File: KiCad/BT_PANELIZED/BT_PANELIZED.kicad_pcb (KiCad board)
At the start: 4 copper layers, 82 x 63.6 mm, 482 parts, among them J1 UJC-HP-3-SMT-TR, J2 2328702-8, J3 Conn_01x05, SW1 Val**, U1 QFN40P120X130X45-6N, U2 SON95P300X300X100-7N-D, U3 STM6601CQ2BDM6F, U4 BMD-350-A-R, U5 UDFN6, U6 UDFN6, U7 UDFN6, Y1 ECS-.327-7-34R-TR

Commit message: updated
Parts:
- removed the C10 at (113.7, 57.4)
- removed the C10 at (148.2, 57.4)
- removed the C10 at (113.7, 74.2)
- removed the C10 at (148.2, 40.6)
- removed the C10 at (113.7, 40.6)
- removed the C10 at (148.2, 74.2)
- removed the C12 at (113.7, 39.6)
- removed the C12 at (148.2, 39.6)
- removed the C12 at (113.7, 73.1)
- removed the C12 at (148.2, 73.1)
- removed the C12 at (148.2, 56.3)
- removed the C12 at (113.7, 56.3)
- removed the C13 at (113.7, 72.0)
- removed the C13 at (148.2, 38.5)
- removed the C13 at (113.7, 38.5)
- removed the C13 at (148.2, 72.0)
- removed the C13 at (113.7, 55.2)
- removed the C13 at (148.2, 55.2)
- removed the C2 at (120.7, 55.7)
- removed the C2 at (155.2, 38.9)
- removed the C2 at (155.2, 72.4)
- removed the C2 at (120.7, 72.4)
- removed the C2 at (120.7, 38.9)
- removed the C2 at (155.2, 55.7)
- removed the C8 at (146.2, 57.5)
- removed the C8 at (111.7, 57.5)
- removed the C8 at (111.7, 74.2)
- removed the C8 at (146.2, 40.7)
- removed the C8 at (146.2, 74.2)
- removed the C8 at (111.7, 40.7)
- removed the C9 at (109.7, 40.7)
- removed the C9 at (144.2, 57.5)
- removed the C9 at (144.2, 74.2)
- removed the C9 at (109.7, 74.2)
- removed the C9 at (109.7, 57.5)
- removed the C9 at (144.2, 40.7)
- removed the D3 at (126.9, 50.6)
- removed the D3 at (126.9, 84.2)
- removed the D3 at (161.4, 84.2)
- removed the D3 at (161.4, 67.4)
- removed the D3 at (126.9, 67.4)
- removed the D3 at (161.4, 50.6)
- removed the J2 at (129.5, 39.4)
- removed the J2 at (164.0, 39.4)
- removed the J2 at (129.5, 72.9)
- removed the J2 at (164.0, 72.9)
- removed the J2 at (164.0, 56.2)
- removed the J2 at (129.5, 56.2)
- removed the R10 at (150.8, 38.9)
- removed the R10 at (116.3, 38.9)
- removed the R10 at (150.8, 72.4)
- removed the R10 at (116.3, 72.4)
- removed the R10 at (116.3, 55.6)
- removed the R10 at (150.8, 55.6)
- removed the R13 at (160.7, 55.6)
- removed the R13 at (126.2, 72.4)
- removed the R13 at (126.2, 55.6)
- removed the R13 at (160.7, 72.4)
- removed the R13 at (126.2, 38.9)
- removed the R13 at (160.7, 38.9)
- removed the R16 at (158.5, 72.4)
- removed the R16 at (124.0, 72.4)
- removed the R16 at (158.5, 55.6)
- removed the R16 at (124.0, 38.9)
- removed the R16 at (158.5, 38.9)
- removed the R16 at (124.0, 55.6)
- removed the R17 at (129.7, 61.7)
- removed the R17 at (164.2, 61.7)
- removed the R17 at (129.7, 78.5)
- removed the R17 at (164.2, 78.5)
- removed the R17 at (164.2, 45.0)
- removed the R17 at (129.7, 45.0)
- removed the R18 at (131.6, 45.0)
- removed the R18 at (131.6, 78.5)
- removed the R18 at (131.6, 61.7)
- removed the R18 at (166.1, 45.0)
- removed the R18 at (166.1, 61.7)
- removed the R18 at (166.1, 78.5)
- removed the R19 at (164.6, 50.7)
- removed the R19 at (164.6, 67.5)
- removed the R19 at (164.6, 84.2)
- removed the R19 at (130.1, 84.2)
- removed the R19 at (130.1, 50.7)
- removed the R19 at (130.1, 67.5)
- removed the R20 at (151.9, 55.6)
- removed the R20 at (117.4, 72.4)
- removed the R20 at (117.4, 38.9)
- removed the R20 at (117.4, 55.6)
- removed the R20 at (151.9, 72.4)
- removed the R20 at (151.9, 38.9)
- removed the R22 at (161.8, 38.9)
- removed the R22 at (161.8, 72.4)
- removed the R22 at (127.3, 72.4)
- removed the R22 at (127.3, 55.6)
- removed the R22 at (127.3, 38.9)
- removed the R22 at (161.8, 55.6)
- removed the R24 at (156.3, 55.6)
- removed the R24 at (121.8, 72.4)
- removed the R24 at (121.8, 38.9)
- removed the R24 at (121.8, 55.6)
- removed the R24 at (156.3, 38.9)
- removed the R24 at (156.3, 72.4)
- removed the R25 at (159.6, 38.9)
- removed the R25 at (125.1, 38.9)
- removed the R25 at (159.6, 55.6)
- removed the R25 at (159.6, 72.4)
- removed the R25 at (125.1, 55.6)
- removed the R25 at (125.1, 72.4)
- removed the R26 at (122.9, 72.4)
- removed the R26 at (157.4, 72.4)
- removed the R26 at (122.9, 38.9)
- removed the R26 at (122.9, 55.6)
- removed the R26 at (157.4, 55.6)
- removed the R26 at (157.4, 38.9)
- removed the R3 at (153.0, 55.6)
- removed the R3 at (118.5, 38.9)
- removed the R3 at (118.5, 55.6)
- removed the R3 at (118.5, 72.4)
- removed the R3 at (153.0, 72.4)
- removed the R3 at (153.0, 38.9)
- removed the R4 at (119.6, 55.6)
- removed the R4 at (154.1, 55.6)
- removed the R4 at (119.6, 72.4)
- removed the R4 at (154.1, 72.4)
- removed the R4 at (119.6, 38.9)
- removed the R4 at (154.1, 38.9)
- removed the R5 at (128.0, 50.7)
- removed the R5 at (162.5, 84.2)
- removed the R5 at (162.5, 50.7)
- removed the R5 at (128.0, 84.2)
- removed the R5 at (162.5, 67.5)
- removed the R5 at (128.0, 67.5)
- removed the R8 at (160.3, 50.7)
- removed the R8 at (125.8, 84.2)
- removed the R8 at (125.8, 67.5)
- removed the R8 at (125.8, 50.7)
- removed the R8 at (160.3, 84.2)
- removed the R8 at (160.3, 67.5)
- removed the R9 at (115.2, 55.6)
- removed the R9 at (149.7, 72.4)
- removed the R9 at (115.2, 38.9)
- removed the R9 at (149.7, 55.6)
- removed the R9 at (149.7, 38.9)
- removed the R9 at (115.2, 72.4)
- removed the U2 at (126.7, 47.5)
- removed the U2 at (126.7, 64.3)
- removed the U2 at (161.2, 47.5)
- removed the U2 at (161.2, 81.0)
- removed the U2 at (161.2, 64.3)
- removed the U2 at (126.7, 81.0)
- removed the Y1 at (145.2, 39.4)
- removed the Y1 at (110.7, 56.2)
- removed the Y1 at (145.2, 72.9)
- removed the Y1 at (110.7, 39.4)
- removed the Y1 at (110.7, 72.9)
- removed the Y1 at (145.2, 56.2)
- added C10: 1uF, Capacitor_Taiyo_Yuden_0402:Capacitor_Taiyo_Yuden_0402, F.Cu at (148.2, 74.2)
- added C10: 1uF, Capacitor_Taiyo_Yuden_0402:Capacitor_Taiyo_Yuden_0402, F.Cu at (113.7, 40.7)
- added C10: 1uF, Capacitor_Taiyo_Yuden_0402:Capacitor_Taiyo_Yuden_0402, F.Cu at (148.2, 40.7)
- added C10: 1uF, Capacitor_Taiyo_Yuden_0402:Capacitor_Taiyo_Yuden_0402, F.Cu at (113.7, 74.2)
- added C10: 1uF, Capacitor_Taiyo_Yuden_0402:Capacitor_Taiyo_Yuden_0402, F.Cu at (113.7, 57.4)
- added C10: 1uF, Capacitor_Taiyo_Yuden_0402:Capacitor_Taiyo_Yuden_0402, F.Cu at (148.2, 57.4)
- added C12: 10nF, Capacitor_Taiyo_Yuden_0402:Capacitor_Taiyo_Yuden_0402, F.Cu at (113.7, 56.4)
- added C12: 10nF, Capacitor_Taiyo_Yuden_0402:Capacitor_Taiyo_Yuden_0402, F.Cu at (148.2, 56.4)
- added C12: 10nF, Capacitor_Taiyo_Yuden_0402:Capacitor_Taiyo_Yuden_0402, F.Cu at (148.2, 73.1)
- added C12: 10nF, Capacitor_Taiyo_Yuden_0402:Capacitor_Taiyo_Yuden_0402, F.Cu at (113.7, 73.1)
- added C12: 10nF, Capacitor_Taiyo_Yuden_0402:Capacitor_Taiyo_Yuden_0402, F.Cu at (148.2, 39.6)
- added C12: 10nF, Capacitor_Taiyo_Yuden_0402:Capacitor_Taiyo_Yuden_0402, F.Cu at (113.7, 39.6)
- added C13: 100nF, Capacitor_Taiyo_Yuden_0402:Capacitor_Taiyo_Yuden_0402, F.Cu at (148.2, 55.3)
- added C13: 100nF, Capacitor_Taiyo_Yuden_0402:Capacitor_Taiyo_Yuden_0402, F.Cu at (113.7, 38.5)
- added C13: 100nF, Capacitor_Taiyo_Yuden_0402:Capacitor_Taiyo_Yuden_0402, F.Cu at (148.2, 38.5)
- added C13: 100nF, Capacitor_Taiyo_Yuden_0402:Capacitor_Taiyo_Yuden_0402, F.Cu at (113.7, 72.0)
- added C13: 100nF, Capacitor_Taiyo_Yuden_0402:Capacitor_Taiyo_Yuden_0402, F.Cu at (113.7, 55.3)
- added C13: 100nF, Capacitor_Taiyo_Yuden_0402:Capacitor_Taiyo_Yuden_0402, F.Cu at (148.2, 72.0)
- added C2: 1uF, Capacitor_Taiyo_Yuden_0402:Capacitor_Taiyo_Yuden_0402, F.Cu at (120.7, 39.0)
- added C2: 1uF, Capacitor_Taiyo_Yuden_0402:Capacitor_Taiyo_Yuden_0402, F.Cu at (155.2, 39.0)
- added C2: 1uF, Capacitor_Taiyo_Yuden_0402:Capacitor_Taiyo_Yuden_0402, F.Cu at (120.7, 55.7)
- added C2: 1uF, Capacitor_Taiyo_Yuden_0402:Capacitor_Taiyo_Yuden_0402, F.Cu at (155.2, 72.5)
- added C2: 1uF, Capacitor_Taiyo_Yuden_0402:Capacitor_Taiyo_Yuden_0402, F.Cu at (155.2, 55.7)
- added C2: 1uF, Capacitor_Taiyo_Yuden_0402:Capacitor_Taiyo_Yuden_0402, F.Cu at (120.7, 72.5)
- added C8: 7pF, Capacitor_Taiyo_Yuden_0402:Capacitor_Taiyo_Yuden_0402, F.Cu at (146.2, 57.5)
- added C8: 7pF, Capacitor_Taiyo_Yuden_0402:Capacitor_Taiyo_Yuden_0402, F.Cu at (146.2, 74.2)
- added C8: 7pF, Capacitor_Taiyo_Yuden_0402:Capacitor_Taiyo_Yuden_0402, F.Cu at (111.7, 74.2)
- added C8: 7pF, Capacitor_Taiyo_Yuden_0402:Capacitor_Taiyo_Yuden_0402, F.Cu at (146.2, 40.7)
- added C8: 7pF, Capacitor_Taiyo_Yuden_0402:Capacitor_Taiyo_Yuden_0402, F.Cu at (111.7, 57.5)
- added C8: 7pF, Capacitor_Taiyo_Yuden_0402:Capacitor_Taiyo_Yuden_0402, F.Cu at (111.7, 40.7)
- added C9: 7pF, Capacitor_Taiyo_Yuden_0402:Capacitor_Taiyo_Yuden_0402, F.Cu at (109.7, 40.7)
- added C9: 7pF, Capacitor_Taiyo_Yuden_0402:Capacitor_Taiyo_Yuden_0402, F.Cu at (144.2, 40.7)
- added C9: 7pF, Capacitor_Taiyo_Yuden_0402:Capacitor_Taiyo_Yuden_0402, F.Cu at (109.7, 74.2)
- added C9: 7pF, Capacitor_Taiyo_Yuden_0402:Capacitor_Taiyo_Yuden_0402, F.Cu at (109.7, 57.5)
- added C9: 7pF, Capacitor_Taiyo_Yuden_0402:Capacitor_Taiyo_Yuden_0402, F.Cu at (144.2, 74.2)
- added C9: 7pF, Capacitor_Taiyo_Yuden_0402:Capacitor_Taiyo_Yuden_0402, F.Cu at (144.2, 57.5)
- added D3: ORG, LED_QBLP595:LED_QBLP595, F.Cu at (161.4, 84.1)
- added D3: ORG, LED_QBLP595:LED_QBLP595, F.Cu at (126.9, 50.6)
- added D3: ORG, LED_QBLP595:LED_QBLP595, F.Cu at (126.9, 67.4)
- added D3: ORG, LED_QBLP595:LED_QBLP595, F.Cu at (161.4, 67.4)
- added D3: ORG, LED_QBLP595:LED_QBLP595, F.Cu at (161.4, 50.6)
- added D3: ORG, LED_QBLP595:LED_QBLP595, F.Cu at (126.9, 84.1)
- added J2: 2328702-8, TE_2328702-8:TE_2328702-8, F.Cu at (164.0, 73.0)
- added J2: 2328702-8, TE_2328702-8:TE_2328702-8, F.Cu at (164.0, 56.2)
- added J2: 2328702-8, TE_2328702-8:TE_2328702-8, F.Cu at (129.5, 73.0)
- added J2: 2328702-8, TE_2328702-8:TE_2328702-8, F.Cu at (164.0, 39.5)
- added J2: 2328702-8, TE_2328702-8:TE_2328702-8, F.Cu at (129.5, 56.2)
- added J2: 2328702-8, TE_2328702-8:TE_2328702-8, F.Cu at (129.5, 39.5)
- added R10: 10k, Stackpole_Res_0402:Stackpole_Res_0402, F.Cu at (116.3, 55.7)
- added R10: 10k, Stackpole_Res_0402:Stackpole_Res_0402, F.Cu at (150.8, 72.5)
- added R10: 10k, Stackpole_Res_0402:Stackpole_Res_0402, F.Cu at (116.3, 39.0)
- added R10: 10k, Stackpole_Res_0402:Stackpole_Res_0402, F.Cu at (150.8, 55.7)
- added R10: 10k, Stackpole_Res_0402:Stackpole_Res_0402, F.Cu at (116.3, 72.5)
- added R10: 10k, Stackpole_Res_0402:Stackpole_Res_0402, F.Cu at (150.8, 39.0)
- added R13: 100k, Stackpole_Res_0402:Stackpole_Res_0402, F.Cu at (160.7, 39.0)
- added R13: 100k, Stackpole_Res_0402:Stackpole_Res_0402, F.Cu at (126.2, 39.0)
- added R13: 100k, Stackpole_Res_0402:Stackpole_Res_0402, F.Cu at (126.2, 72.5)
- added R13: 100k, Stackpole_Res_0402:Stackpole_Res_0402, F.Cu at (126.2, 55.7)
- added R13: 100k, Stackpole_Res_0402:Stackpole_Res_0402, F.Cu at (160.7, 72.5)
- added R13: 100k, Stackpole_Res_0402:Stackpole_Res_0402, F.Cu at (160.7, 55.7)
- added R16: 100k, Stackpole_Res_0402:Stackpole_Res_0402, F.Cu at (124.0, 55.7)
- added R16: 100k, Stackpole_Res_0402:Stackpole_Res_0402, F.Cu at (158.5, 72.5)
- added R16: 100k, Stackpole_Res_0402:Stackpole_Res_0402, F.Cu at (158.5, 55.7)
- added R16: 100k, Stackpole_Res_0402:Stackpole_Res_0402, F.Cu at (124.0, 72.5)
- added R16: 100k, Stackpole_Res_0402:Stackpole_Res_0402, F.Cu at (124.0, 39.0)
- added R16: 100k, Stackpole_Res_0402:Stackpole_Res_0402, F.Cu at (158.5, 39.0)
- added R17: 4.7k, Stackpole_Res_0402:Stackpole_Res_0402, F.Cu at (164.2, 78.5)
- added R17: 4.7k, Stackpole_Res_0402:Stackpole_Res_0402, F.Cu at (164.2, 61.8)
- added R17: 4.7k, Stackpole_Res_0402:Stackpole_Res_0402, F.Cu at (164.2, 45.0)
- added R17: 4.7k, Stackpole_Res_0402:Stackpole_Res_0402, F.Cu at (129.7, 78.5)
- added R17: 4.7k, Stackpole_Res_0402:Stackpole_Res_0402, F.Cu at (129.7, 61.8)
- added R17: 4.7k, Stackpole_Res_0402:Stackpole_Res_0402, F.Cu at (129.7, 45.0)
- added R18: 4.7k, Stackpole_Res_0402:Stackpole_Res_0402, F.Cu at (166.1, 78.5)
- added R18: 4.7k, Stackpole_Res_0402:Stackpole_Res_0402, F.Cu at (131.6, 45.0)
- added R18: 4.7k, Stackpole_Res_0402:Stackpole_Res_0402, F.Cu at (131.6, 78.5)
- added R18: 4.7k, Stackpole_Res_0402:Stackpole_Res_0402, F.Cu at (166.1, 61.8)
- added R18: 4.7k, Stackpole_Res_0402:Stackpole_Res_0402, F.Cu at (166.1, 45.0)
- added R18: 4.7k, Stackpole_Res_0402:Stackpole_Res_0402, F.Cu at (131.6, 61.8)
- added R19: 10k, Stackpole_Res_0402:Stackpole_Res_0402, F.Cu at (164.6, 50.7)
- added R19: 10k, Stackpole_Res_0402:Stackpole_Res_0402, F.Cu at (130.1, 67.4)
- added R19: 10k, Stackpole_Res_0402:Stackpole_Res_0402, F.Cu at (130.1, 84.2)
- added R19: 10k, Stackpole_Res_0402:Stackpole_Res_0402, F.Cu at (130.1, 50.7)
- added R19: 10k, Stackpole_Res_0402:Stackpole_Res_0402, F.Cu at (164.6, 67.4)
- added R19: 10k, Stackpole_Res_0402:Stackpole_Res_0402, F.Cu at (164.6, 84.2)
- added R20: 10k, Stackpole_Res_0402:Stackpole_Res_0402, F.Cu at (151.9, 55.7)
- added R20: 10k, Stackpole_Res_0402:Stackpole_Res_0402, F.Cu at (117.4, 55.7)
- added R20: 10k, Stackpole_Res_0402:Stackpole_Res_0402, F.Cu at (117.4, 72.5)
- added R20: 10k, Stackpole_Res_0402:Stackpole_Res_0402, F.Cu at (117.4, 39.0)
- added R20: 10k, Stackpole_Res_0402:Stackpole_Res_0402, F.Cu at (151.9, 72.5)
- added R20: 10k, Stackpole_Res_0402:Stackpole_Res_0402, F.Cu at (151.9, 39.0)
- added R22: 100k, Stackpole_Res_0402:Stackpole_Res_0402, F.Cu at (161.8, 39.0)
- added R22: 100k, Stackpole_Res_0402:Stackpole_Res_0402, F.Cu at (161.8, 72.5)
- added R22: 100k, Stackpole_Res_0402:Stackpole_Res_0402, F.Cu at (127.3, 72.5)
- added R22: 100k, Stackpole_Res_0402:Stackpole_Res_0402, F.Cu at (161.8, 55.7)
- added R22: 100k, Stackpole_Res_0402:Stackpole_Res_0402, F.Cu at (127.3, 39.0)
- added R22: 100k, Stackpole_Res_0402:Stackpole_Res_0402, F.Cu at (127.3, 55.7)
- added R24: 1k, Stackpole_Res_0402:Stackpole_Res_0402, F.Cu at (121.8, 72.5)
- added R24: 1k, Stackpole_Res_0402:Stackpole_Res_0402, F.Cu at (156.3, 55.7)
- added R24: 1k, Stackpole_Res_0402:Stackpole_Res_0402, F.Cu at (121.8, 39.0)
- added R24: 1k, Stackpole_Res_0402:Stackpole_Res_0402, F.Cu at (156.3, 39.0)
- added R24: 1k, Stackpole_Res_0402:Stackpole_Res_0402, F.Cu at (156.3, 72.5)
- added R24: 1k, Stackpole_Res_0402:Stackpole_Res_0402, F.Cu at (121.8, 55.7)
- added R25: 1k, Stackpole_Res_0402:Stackpole_Res_0402, F.Cu at (125.1, 55.7)
- added R25: 1k, Stackpole_Res_0402:Stackpole_Res_0402, F.Cu at (125.1, 39.0)
- added R25: 1k, Stackpole_Res_0402:Stackpole_Res_0402, F.Cu at (159.6, 72.5)
- added R25: 1k, Stackpole_Res_0402:Stackpole_Res_0402, F.Cu at (125.1, 72.5)
- added R25: 1k, Stackpole_Res_0402:Stackpole_Res_0402, F.Cu at (159.6, 39.0)
- added R25: 1k, Stackpole_Res_0402:Stackpole_Res_0402, F.Cu at (159.6, 55.7)
- added R26: 100k, Stackpole_Res_0402:Stackpole_Res_0402, F.Cu at (157.4, 55.7)
- added R26: 100k, Stackpole_Res_0402:Stackpole_Res_0402, F.Cu at (122.9, 39.0)
- added R26: 100k, Stackpole_Res_0402:Stackpole_Res_0402, F.Cu at (157.4, 72.5)
- added R26: 100k, Stackpole_Res_0402:Stackpole_Res_0402, F.Cu at (122.9, 72.5)
- added R26: 100k, Stackpole_Res_0402:Stackpole_Res_0402, F.Cu at (122.9, 55.7)
- added R26: 100k, Stackpole_Res_0402:Stackpole_Res_0402, F.Cu at (157.4, 39.0)
- added R3: 75k (1%), Stackpole_Res_0402:Stackpole_Res_0402, F.Cu at (153.0, 39.0)
- added R3: 75k (1%), Stackpole_Res_0402:Stackpole_Res_0402, F.Cu at (118.5, 55.7)
- added R3: 75k (1%), Stackpole_Res_0402:Stackpole_Res_0402, F.Cu at (153.0, 55.7)
- added R3: 75k (1%), Stackpole_Res_0402:Stackpole_Res_0402, F.Cu at (153.0, 72.5)
- added R3: 75k (1%), Stackpole_Res_0402:Stackpole_Res_0402, F.Cu at (118.5, 39.0)
- added R3: 75k (1%), Stackpole_Res_0402:Stackpole_Res_0402, F.Cu at (118.5, 72.5)
- added R4: 30k (1%), Stackpole_Res_0402:Stackpole_Res_0402, F.Cu at (154.1, 72.5)
- added R4: 30k (1%), Stackpole_Res_0402:Stackpole_Res_0402, F.Cu at (154.1, 55.7)
- added R4: 30k (1%), Stackpole_Res_0402:Stackpole_Res_0402, F.Cu at (119.6, 55.7)
- added R4: 30k (1%), Stackpole_Res_0402:Stackpole_Res_0402, F.Cu at (154.1, 39.0)
- added R4: 30k (1%), Stackpole_Res_0402:Stackpole_Res_0402, F.Cu at (119.6, 72.5)
- added R4: 30k (1%), Stackpole_Res_0402:Stackpole_Res_0402, F.Cu at (119.6, 39.0)
- added R5: 10k, Stackpole_Res_0402:Stackpole_Res_0402, F.Cu at (128.0, 50.7)
- added R5: 10k, Stackpole_Res_0402:Stackpole_Res_0402, F.Cu at (128.0, 67.4)
- added R5: 10k, Stackpole_Res_0402:Stackpole_Res_0402, F.Cu at (162.5, 84.2)
- added R5: 10k, Stackpole_Res_0402:Stackpole_Res_0402, F.Cu at (128.0, 84.2)
- added R5: 10k, Stackpole_Res_0402:Stackpole_Res_0402, F.Cu at (162.5, 67.4)
- added R5: 10k, Stackpole_Res_0402:Stackpole_Res_0402, F.Cu at (162.5, 50.7)
- added R8: 10k (1%), Stackpole_Res_0402:Stackpole_Res_0402, F.Cu at (125.8, 50.7)
- added R8: 10k (1%), Stackpole_Res_0402:Stackpole_Res_0402, F.Cu at (160.3, 84.2)
- added R8: 10k (1%), Stackpole_Res_0402:Stackpole_Res_0402, F.Cu at (125.8, 67.4)
- added R8: 10k (1%), Stackpole_Res_0402:Stackpole_Res_0402, F.Cu at (160.3, 50.7)
- added R8: 10k (1%), Stackpole_Res_0402:Stackpole_Res_0402, F.Cu at (125.8, 84.2)
- added R8: 10k (1%), Stackpole_Res_0402:Stackpole_Res_0402, F.Cu at (160.3, 67.4)
- added R9: 10k, Stackpole_Res_0402:Stackpole_Res_0402, F.Cu at (149.7, 39.0)
- added R9: 10k, Stackpole_Res_0402:Stackpole_Res_0402, F.Cu at (115.2, 72.5)
- added R9: 10k, Stackpole_Res_0402:Stackpole_Res_0402, F.Cu at (149.7, 72.5)
- added R9: 10k, Stackpole_Res_0402:Stackpole_Res_0402, F.Cu at (115.2, 55.7)
- added R9: 10k, Stackpole_Res_0402:Stackpole_Res_0402, F.Cu at (149.7, 55.7)
- added R9: 10k, Stackpole_Res_0402:Stackpole_Res_0402, F.Cu at (115.2, 39.0)
- added U2: SON95P300X300X100-7N-D, STBC08PMR:STBC08PMR, F.Cu at (126.7, 81.0)
- added U2: SON95P300X300X100-7N-D, STBC08PMR:STBC08PMR, F.Cu at (161.2, 47.5)
- added U2: SON95P300X300X100-7N-D, STBC08PMR:STBC08PMR, F.Cu at (126.7, 47.5)
- added U2: SON95P300X300X100-7N-D, STBC08PMR:STBC08PMR, F.Cu at (161.2, 81.0)
- added U2: SON95P300X300X100-7N-D, STBC08PMR:STBC08PMR, F.Cu at (161.2, 64.3)
- added U2: SON95P300X300X100-7N-D, STBC08PMR:STBC08PMR, F.Cu at (126.7, 64.3)
- added Y1: ECS-.327-7-34R-TR, ECS-.327-7-34R-TR:XTAL_ECS-.327-CDX-2216, F.Cu at (145.2, 56.2)
- added Y1: ECS-.327-7-34R-TR, ECS-.327-7-34R-TR:XTAL_ECS-.327-CDX-2216, F.Cu at (145.2, 39.4)
- added Y1: ECS-.327-7-34R-TR, ECS-.327-7-34R-TR:XTAL_ECS-.327-CDX-2216, F.Cu at (110.7, 56.2)
- added Y1: ECS-.327-7-34R-TR, ECS-.327-7-34R-TR:XTAL_ECS-.327-CDX-2216, F.Cu at (110.7, 72.9)
- added Y1: ECS-.327-7-34R-TR, ECS-.327-7-34R-TR:XTAL_ECS-.327-CDX-2216, F.Cu at (145.2, 72.9)
- added Y1: ECS-.327-7-34R-TR, ECS-.327-7-34R-TR:XTAL_ECS-.327-CDX-2216, F.Cu at (110.7, 39.4)
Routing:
- net GND: track 244.1 -> 240.7 mm, vias 414 -> 420
- net XSHUT2: track 147.4 -> 145.0 mm
- net VUSB: track 166.6 -> 164.3 mm
- net VBUS: track 172.8 -> 170.7 mm
- net PROG: track 67.3 -> 69.4 mm
- net CHRG: track 61.9 -> 60.4 mm
- net PWR_ON: track 127.2 -> 128.3 mm
- net SCL: track 143.0 -> 141.9 mm
- net PS_HOLD: track 55.8 -> 55.0 mm
- net Net-(U1-BYP/ADJ/NC): track 16.4 -> 15.8 mm
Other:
- board text added: "BT_v6.1"
- board text removed: "BT_v6.0"

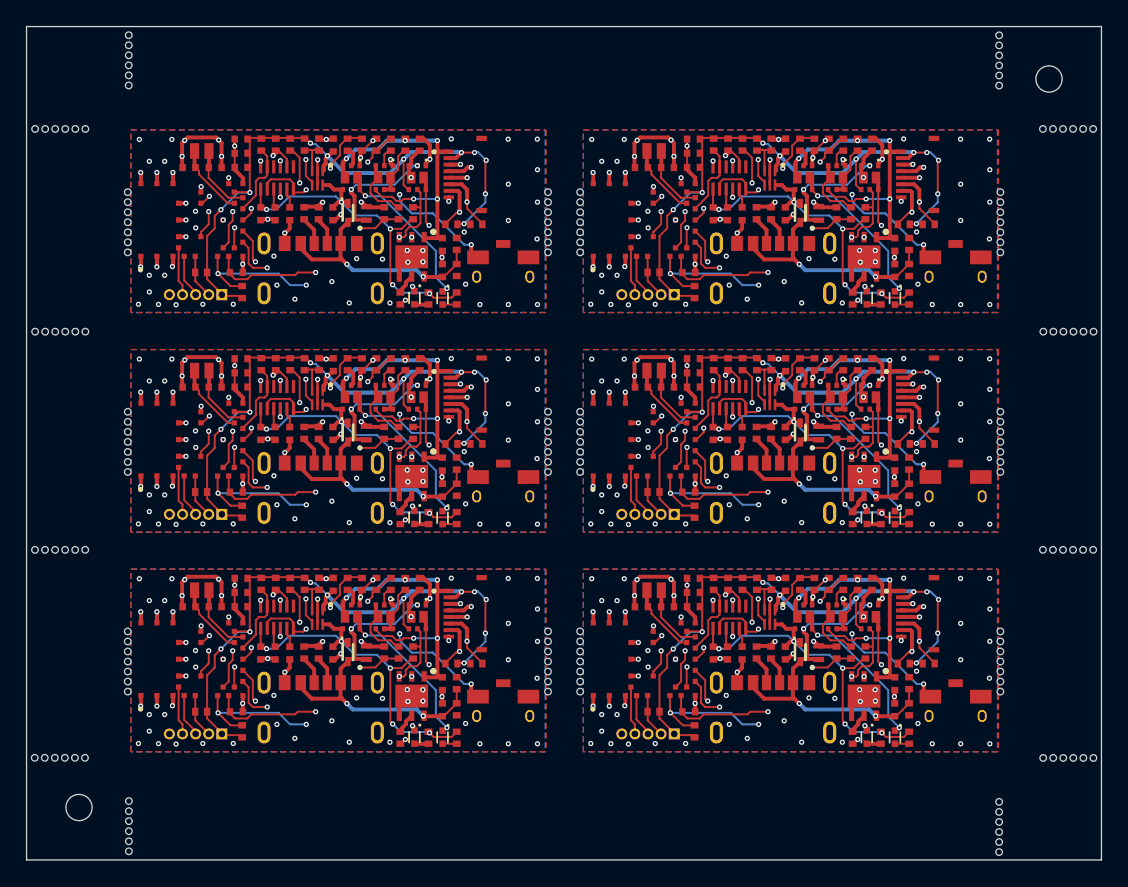
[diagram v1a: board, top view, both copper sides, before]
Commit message: swapped SWDIO/SWCLK, BM pin moved to AN4
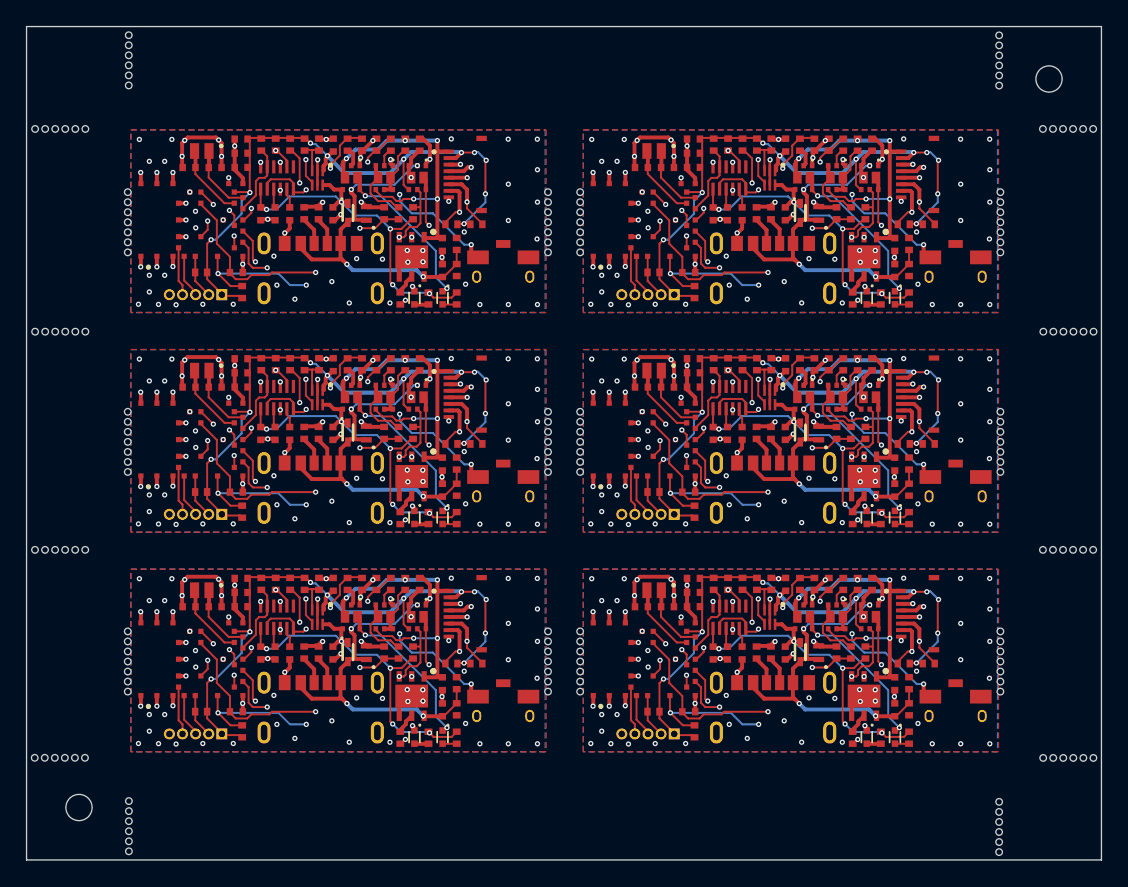
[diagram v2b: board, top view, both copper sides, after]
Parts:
- removed the D2 at (163.6, 67.4)
- removed the D2 at (129.1, 84.2)
- removed the D2 at (129.1, 67.4)
- removed the D2 at (129.1, 50.6)
- removed the D2 at (163.6, 50.6)
- removed the D2 at (163.6, 84.2)
- added D2: YEL/GRN, LED_QBLP595:LED_QBLP595, F.Cu at (163.6, 50.6)
- added D2: YEL/GRN, LED_QBLP595:LED_QBLP595, F.Cu at (163.6, 67.4)
- added D2: YEL/GRN, LED_QBLP595:LED_QBLP595, F.Cu at (129.1, 84.1)
- added D2: YEL/GRN, LED_QBLP595:LED_QBLP595, F.Cu at (129.1, 67.4)
- added D2: YEL/GRN, LED_QBLP595:LED_QBLP595, F.Cu at (129.1, 50.6)
- added D2: YEL/GRN, LED_QBLP595:LED_QBLP595, F.Cu at (163.6, 84.1)
- SW1 (x6): value Val** -> PTS840ESDPMSMTRLFS
- U1 (x6): value QFN40P120X130X45-6N -> LDK130PU-R
- U2 (x6): value SON95P300X300X100-7N-D -> STBC08PMR
- U5 (x6), U6 (x6), U7 (x6): value UDFN6 -> SSM6L61NU
- Y1 (x6): value ECS-.327-7-34R-TR -> ECS-.327-CDX-2216
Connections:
- J3 pad 3: SWDCLK -> SWDIO (x6)
- J3 pad 4: SWDIO -> SWDCLK (x6)
- U4 pad 32: LED_EN -> BM_EN (x6)
- U4 pad 4: SWDIO -> SWDCLK (x6)
- U4 pad 45: BM_EN -> BM (x6)
- U4 pad 5: SWDCLK -> SWDIO (x6)
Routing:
- net BM: track 97.9 -> 127.3 mm
- net XSHUT1: track 145.2 -> 134.7 mm
- net PS_HOLD: track 55.0 -> 50.7 mm
- net GND: track 240.7 -> 237.2 mm
- net SWDIO: track 22.1 -> 19.7 mm
- net SWDCLK: track 19.7 -> 22.1 mm
- net BM_EN: track 102.2 -> 104.6 mm
- net CHRG_STAT: track 131.7 -> 129.4 mm
- net XSHUT2: track 145.0 -> 142.9 mm
- net V2.8: track 299.7 -> 297.8 mm
- net LED_EN: track 92.1 -> 93.6 mm
- net PROG: track 69.4 -> 67.9 mm
- net VBATT: track 145.3 -> 143.8 mm
- net VUSB: track 164.3 -> 163.0 mm
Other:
- board text added: "BT_v7.0"
- board text removed: "BT_v6.1"
